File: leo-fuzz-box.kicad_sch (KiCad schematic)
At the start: 14 parts, among them Q1 2N3565, Q2 2N3565

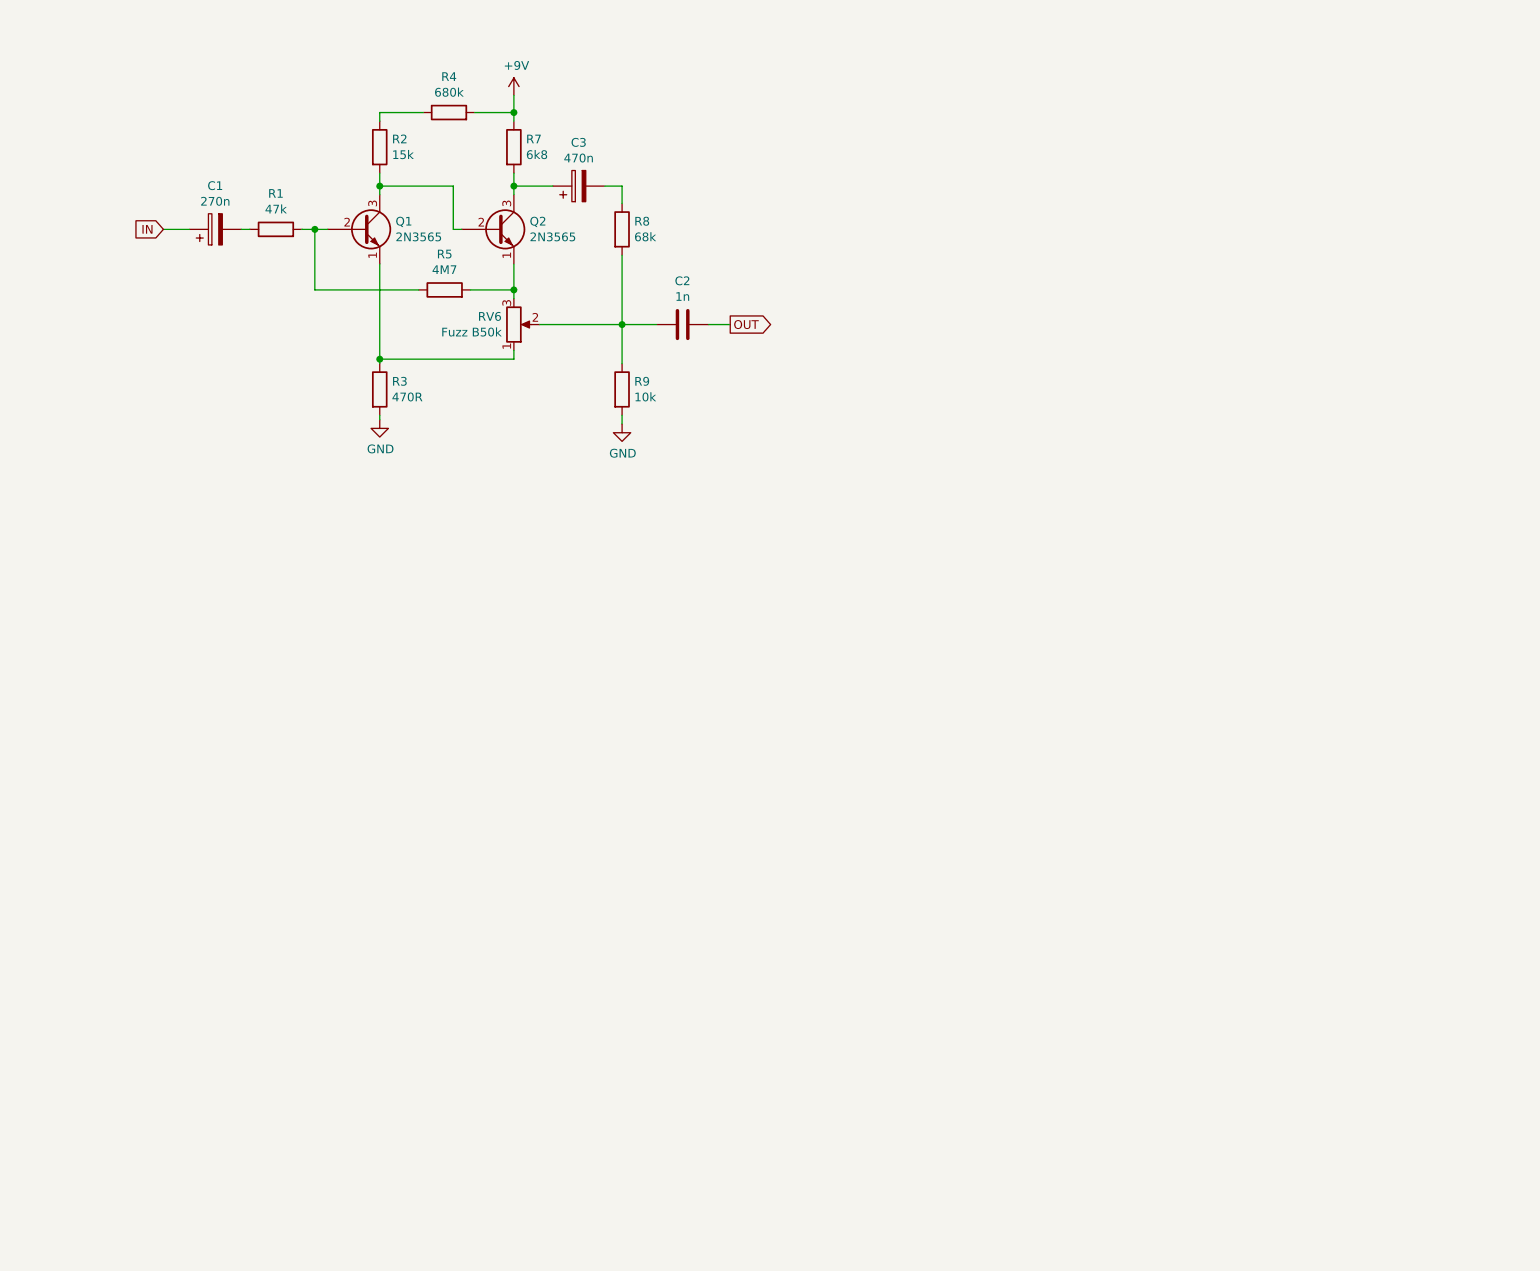
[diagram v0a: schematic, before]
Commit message: added power protection, finished first version of pcb layout
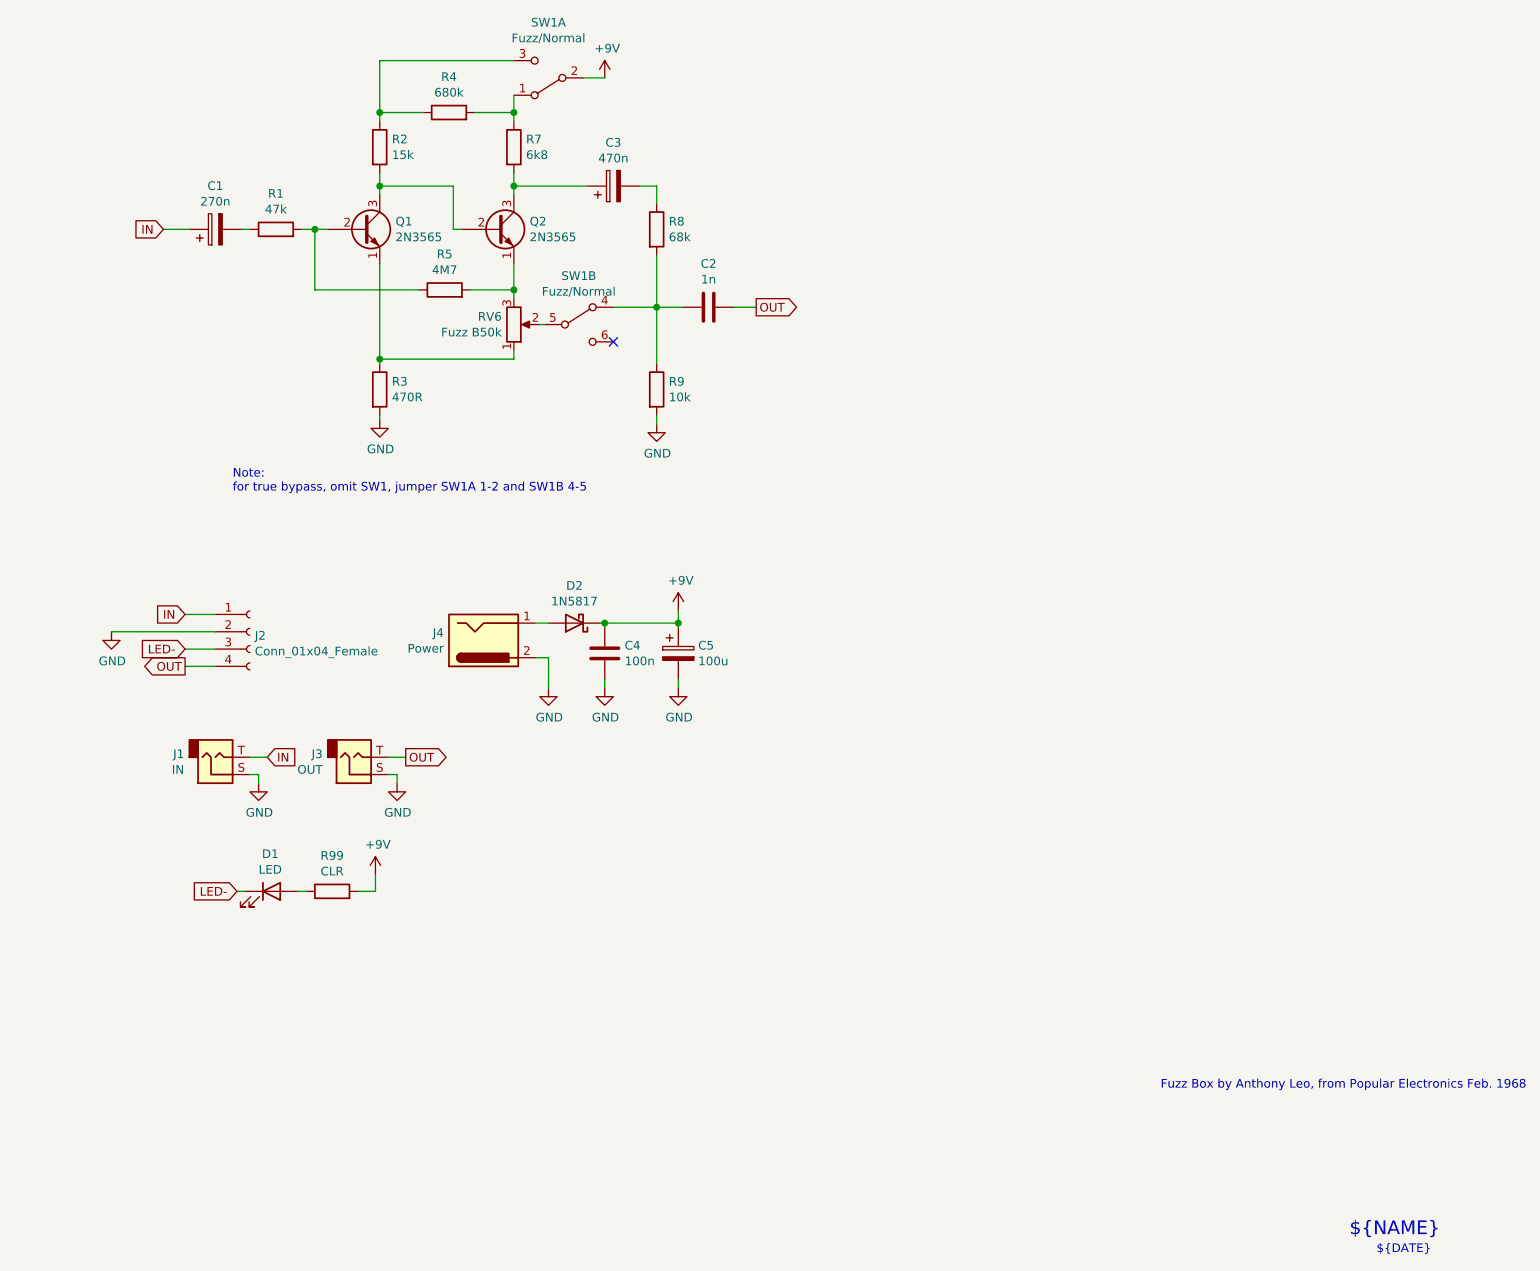
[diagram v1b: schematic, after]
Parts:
- added C4: 100n, rockola_kicad_footprints:C_Box_7.2_2.5, symbol Device:C
- added C5: 100u, rockola_kicad_footprints:CP_D5.0_P2.50, symbol Device:CP
- added D1: LED, rockola_kicad_footprints:LED.3mm, symbol Device:LED
- added D2: 1N5817, Diode_THT:D_DO-41_SOD81_P10.16mm_Horizontal, symbol Diode:1N5817
- added J1: IN, rockola_kicad_footprints:2PADS_TipSleeve, symbol Connector:AudioJack2
- added J2: Conn_01x04_Female, rockola_kicad_footprints:Stomp_4pin, symbol Connector:Conn_01x04_Female
- added J3: OUT, rockola_kicad_footprints:2PADS_TipSleeve, symbol Connector:AudioJack2
- added J4: Power, rockola_kicad_footprints:Power_Header_2pin, symbol rockola_symbols:Power_Pedal_BarrelJack
- added R99: CLR, rockola_kicad_footprints:R_DIN0207, symbol Device:R
- added SW1: Fuzz/Normal, switches:DPDT.WIRE, symbol Switch:SW_DPDT_x2
- C1, C2, C3: footprint (none) -> rockola_kicad_footprints:C_Box_7.2_2.5
- Q1, Q2: footprint Package_TO_SOT_THT:TO-39-3 -> rockola_kicad_footprints:TO92
- R1, R2, R3, R4, R5, R7, R8, R9: footprint (none) -> rockola_kicad_footprints:R_DIN0207
- RV6: footprint (none) -> potentiometers:16MM_B.MOUNT
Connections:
- net +9V: now also C4.1, C5.1, D2.1 (K), R99.2, SW1.2 (B); no longer R4.2, R7.1
- net GND: now also C4.2, C5.2, J1.S, J2.2 (Pin_2), J3.S, J4.2
- net IN: now also J1.T, J2.1 (Pin_1)
- net OUT: now also J2.4 (Pin_4), J3.T
- net at C2.1, R8.2, R9.1: now also SW1.4 (A); no longer RV6.2
- net at R2.1, R4.1: now also SW1.3 (C)
- new net: D2.2 (A), J4.1
- new net: RV6.2, SW1.5 (B)
- new net: D1.2 (A), R99.1
- new net: R4.2, R7.1, SW1.1 (A)
- new net LED-: D1.1 (K), J2.3 (Pin_3)
- no-connect marks 0 -> 1
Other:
- note added: "${DATE}"
- note added: "${NAME}"
- note added: "${REVISION}"
- note added: "Fuzz Box by Anthony Leo, from Popular Electronics Feb. 1968"
- note added: "Note: for true bypass, omit SW1, jumper SW1A 1-2 and SW1B 4-5"
- moved on the sheet: C2, C3, R8, R9

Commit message: packed tighter but functionally the same
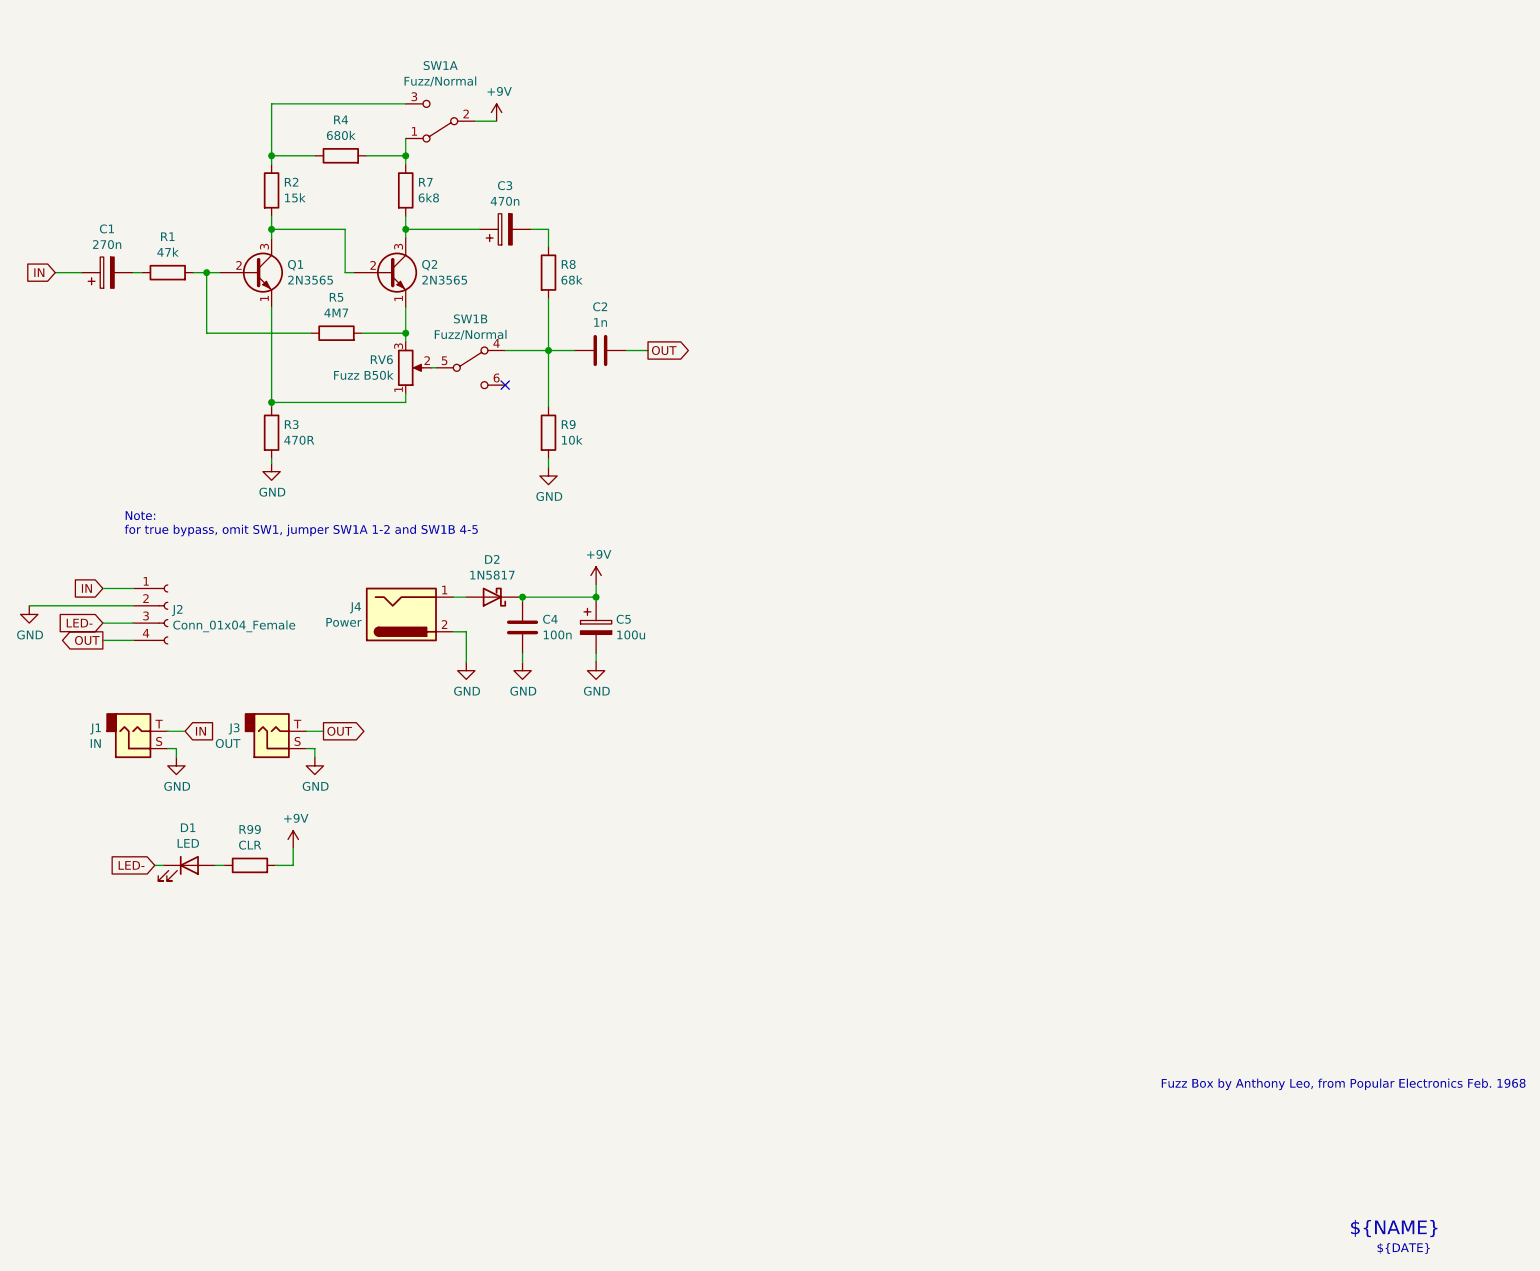
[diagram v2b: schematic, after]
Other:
- moved on the sheet: C1, C2, C3, C4, C5, D1, D2, J1, J2, J3, J4, Q1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
